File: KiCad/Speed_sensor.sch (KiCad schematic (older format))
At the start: 65 parts

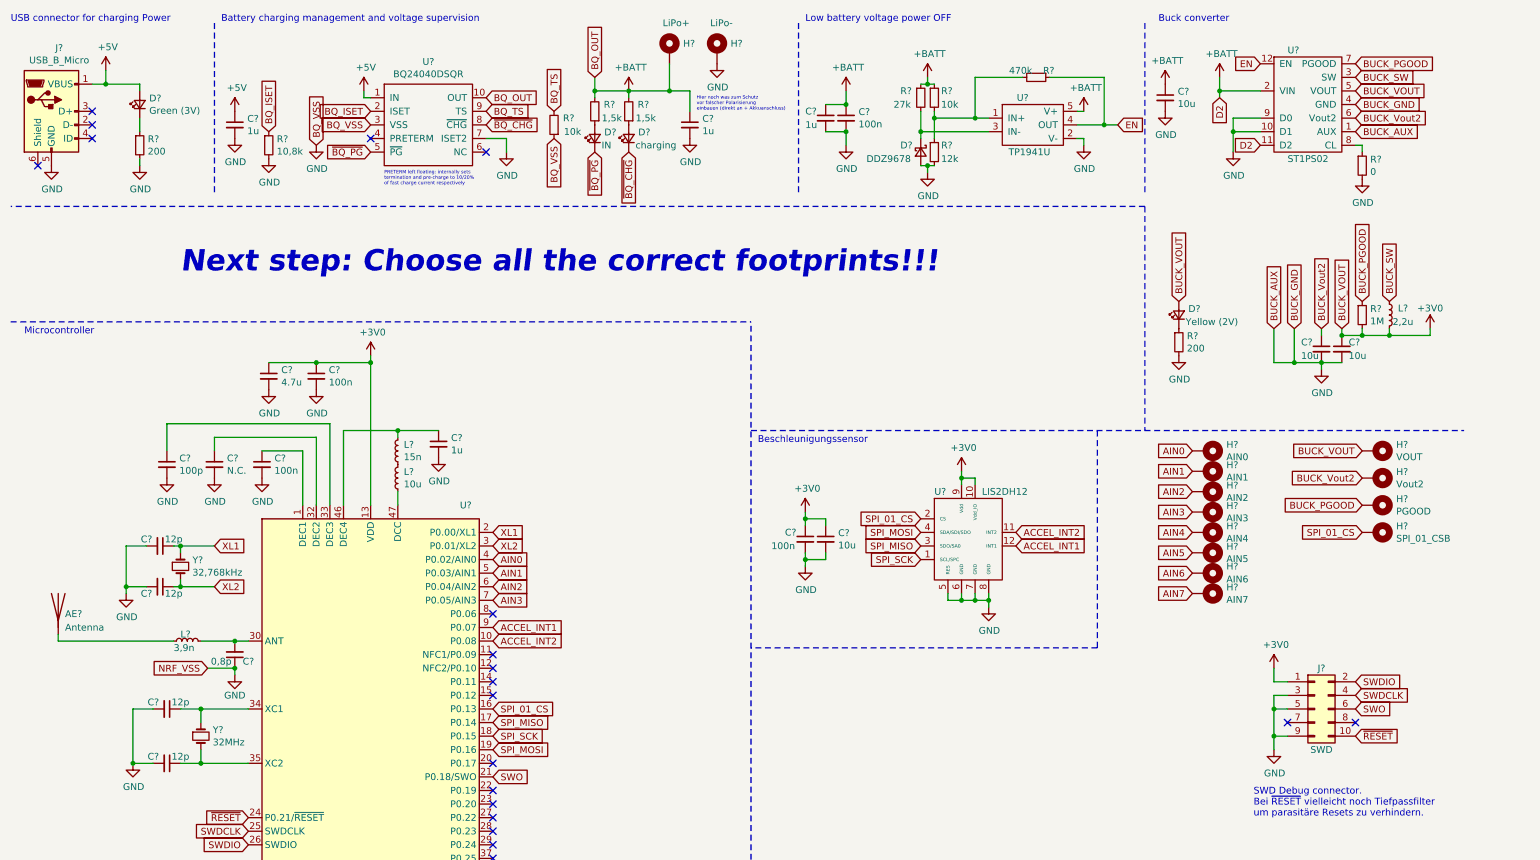
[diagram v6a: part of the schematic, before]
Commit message: added all annotations
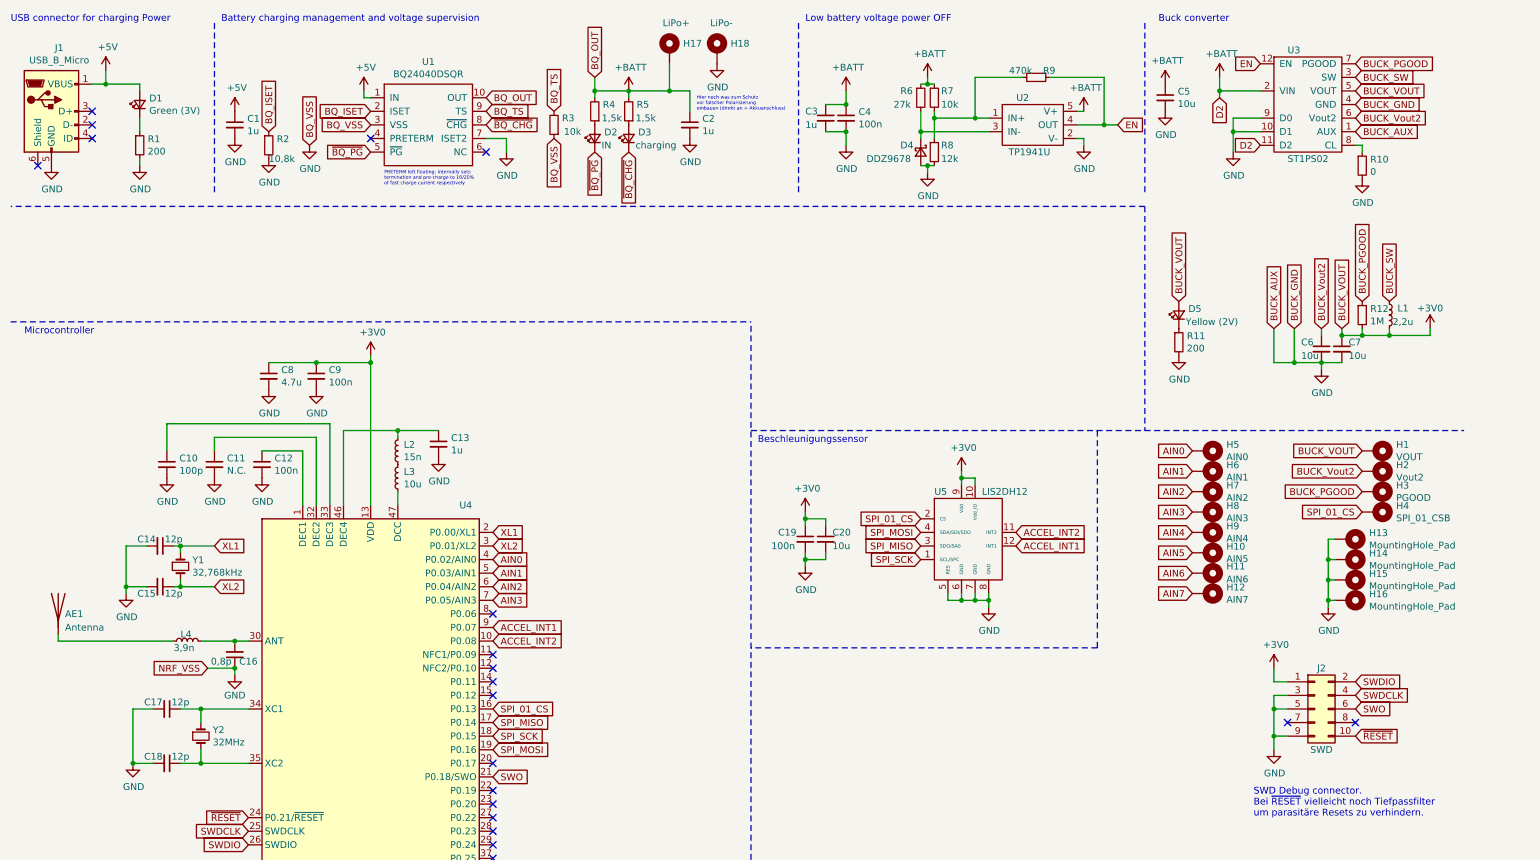
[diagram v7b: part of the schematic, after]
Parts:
- added H13, H14, H15, H16: MountingHole_Pad, symbol Mechanical:MountingHole_Pad
- gave numbers to parts that had none: 65
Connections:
- net GND: now also H13.1, H14.1, H15.1, H16.1
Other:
- note removed: "Next step: Choose all the correct footprints!!!"
- moved on the sheet: H2, H3, H4

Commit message: added a lot of footprints (mainly crystal and all the chips are missing)
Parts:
- removed AE1: Antenna, symbol Device:Antenna
- added C10: 100n, Capacitor_SMD:C_0402_1005Metric_Pad0.74x0.62mm_HandSolder, symbol Device:C_Small
- C1, C2, C3, C4, C5, C6, C7, C8: footprint (none) -> Capacitor_SMD:C_0603_1608Metric_Pad1.08x0.95mm_HandSolder
- C11: renamed from C10; footprint (none) -> Capacitor_SMD:C_0402_1005Metric_Pad0.74x0.62mm_HandSolder
- C12: renamed from C11; footprint (none) -> Capacitor_SMD:C_0402_1005Metric_Pad0.74x0.62mm_HandSolder
- C13: renamed from C12; footprint (none) -> Capacitor_SMD:C_0402_1005Metric_Pad0.74x0.62mm_HandSolder
- C14: renamed from C13; footprint (none) -> Capacitor_SMD:C_0603_1608Metric_Pad1.08x0.95mm_HandSolder
- C15: renamed from C14; footprint (none) -> Capacitor_SMD:C_0402_1005Metric_Pad0.74x0.62mm_HandSolder
- C16: renamed from C15; footprint (none) -> Capacitor_SMD:C_0402_1005Metric_Pad0.74x0.62mm_HandSolder
- C17: renamed from C16; footprint (none) -> Capacitor_SMD:C_0402_1005Metric_Pad0.74x0.62mm_HandSolder
- C18: renamed from C17; footprint (none) -> Capacitor_SMD:C_0402_1005Metric_Pad0.74x0.62mm_HandSolder
- C19: renamed from C18; footprint (none) -> Capacitor_SMD:C_0402_1005Metric_Pad0.74x0.62mm_HandSolder
- C20: renamed from C19; footprint (none) -> Capacitor_SMD:C_0402_1005Metric_Pad0.74x0.62mm_HandSolder
- C21: renamed from C20; footprint (none) -> Capacitor_SMD:C_0603_1608Metric_Pad1.08x0.95mm_HandSolder
- C9: footprint (none) -> Capacitor_SMD:C_0402_1005Metric_Pad0.74x0.62mm_HandSolder
- D1, D2, D3, D5: footprint (none) -> Diode_SMD:D_0603_1608Metric_Pad1.05x0.95mm_HandSolder
- D4: footprint (none) -> Diode_SMD:D_SOD-123
- H1, H10, H11, H12, H2, H3, H4, H5, H6, H7, H8, H9: footprint (none) -> TestPoint:TestPoint_Plated_Hole_D2.0mm
- H13, H14, H15, H16: footprint (none) -> MountingHole:MountingHole_4.3mm_M4_Pad_Via
- H17, H18: footprint (none) -> TestPoint:TestPoint_Plated_Hole_D3.0mm
- J1: footprint (none) -> Connector_USB:USB_Micro-B_Amphenol_10103594-0001LF_Horizontal
- J2: footprint (none) -> Connector_PinSocket_2.00mm:PinSocket_2x05_P2.00mm_Vertical_SMD
- L1: footprint (none) -> Resistor_SMD:R_0805_2012Metric_Pad1.20x1.40mm_HandSolder
- L2, L4: footprint (none) -> Inductor_SMD:L_0402_1005Metric_Pad0.77x0.64mm_HandSolder
- L3: footprint (none) -> Inductor_SMD:L_0603_1608Metric_Pad1.05x0.95mm_HandSolder
- R1, R11, R2, R3, R4, R5: footprint (none) -> Resistor_SMD:R_0603_1608Metric_Pad0.98x0.95mm_HandSolder
- R10, R12, R6, R7, R8, R9: footprint (none) -> Resistor_SMD:R_0402_1005Metric_Pad0.72x0.64mm_HandSolder
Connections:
- net +3V0: now also C10.1
- net GND: now also C10.2
- no-connect marks 22 -> 23
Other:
- moved on the sheet: C8, C9
